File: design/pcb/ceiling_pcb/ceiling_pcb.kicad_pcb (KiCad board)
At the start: 2 copper layers, 60 x 208 mm, 10 parts, among them J1 Conn_01x09, J10 shock_grid, J2 Conn_01x09, J3 shock_grid, J4 shock_grid, J5 shock_grid, J6 shock_grid, J7 shock_grid, J8 shock_grid, J9 shock_grid

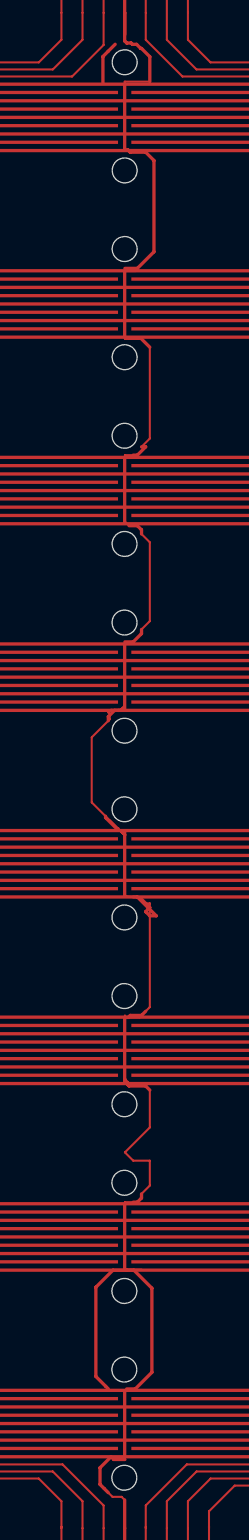
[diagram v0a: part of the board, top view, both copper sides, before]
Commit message: Think ceiling has holes converted to a manufacturable format. Going to do floor now then regenerate output for manufacture.
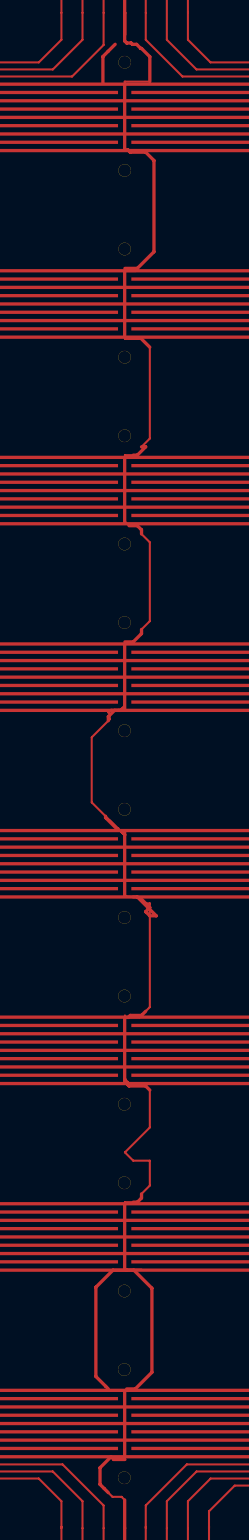
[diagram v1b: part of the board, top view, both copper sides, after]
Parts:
- added R1.5mm_NPTH: , R1.5mm_NPTH, F.Cu at (125.0, 29.7)
- added R1.5mm_NPTH: , R1.5mm_NPTH, F.Cu at (125.0, 132.8)
- added R1.5mm_NPTH: , R1.5mm_NPTH, F.Cu at (125.0, 142.2)
- added R1.5mm_NPTH: , R1.5mm_NPTH, F.Cu at (125.0, 155.3)
- added R1.5mm_NPTH: , R1.5mm_NPTH, F.Cu at (125.0, 164.7)
- added R1.5mm_NPTH: , R1.5mm_NPTH, F.Cu at (125.0, 177.8)
- added R1.5mm_NPTH: , R1.5mm_NPTH, F.Cu at (125.0, 187.2)
- added R1.5mm_NPTH: , R1.5mm_NPTH, F.Cu at (125.0, 200.3)
- added R1.5mm_NPTH: , R1.5mm_NPTH, F.Cu at (125.0, 42.8)
- added R1.5mm_NPTH: , R1.5mm_NPTH, F.Cu at (125.0, 52.2)
- added R1.5mm_NPTH: , R1.5mm_NPTH, F.Cu at (125.0, 65.3)
- added R1.5mm_NPTH: , R1.5mm_NPTH, F.Cu at (125.0, 87.8)
- added R1.5mm_NPTH: , R1.5mm_NPTH, F.Cu at (125.0, 74.7)
- added R1.5mm_NPTH: , R1.5mm_NPTH, F.Cu at (125.0, 97.2)
- added R1.5mm_NPTH: , R1.5mm_NPTH, F.Cu at (125.0, 110.3)
- added R1.5mm_NPTH: , R1.5mm_NPTH, F.Cu at (125.0, 119.7)
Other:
- outline, holes or cut-outs redrawn
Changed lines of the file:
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@@
-(kicad_pcb (version 20170922) (host pcbnew "(2017-11-10 revision d8f4e35)-HEAD")
+(kicad_pcb (version 20171130) (host pcbnew "(2017-12-12 revision 8e764f8)-master")
   (general
     (thickness 1.6)
-    (drawings 24)
+    (drawings 8)
     (tracks 283)
     (zones 0)
-    (modules 10)
+    (modules 26)
     (nets 18)
   )
@@
     (add_net /HV)
   )
+  (module R1.5mm_NPTH locked (layer F.Cu)
+    (at 125.001 29.7452)
+    (tags "non-plated through hole NPTH")
+    (attr virtual)
+    (fp_text reference R1.5mm_NPTH (at 0 0) (layer Cmts.User)
+      (effects (font (thickness 0.15)))
+    )
+    (fp_text value "" (at 0 0) (layer Cmts.User)
+      (effects (font (thickness 0.15)))
+    )
+    (pad 1 np_thru_hole circle (at 0 0) (size 1.524 1.524) (drill 1.5) (layers *.Cu *.Mask))
+  )
+  (module R1.5mm_NPTH locked (layer F.Cu)
+    (at 125.001 42.7792)
+    (tags "non-plated through hole NPTH")
+    (attr virtual)
+    (fp_text reference R1.5mm_NPTH (at 0 0) (layer Cmts.User)
+      (effects (font (thickness 0.15)))
+    )
+    (fp_text value "" (at 0 0) (layer Cmts.User)
+      (effects (font (thickness 0.15)))
+    )
+    (pad 1 np_thru_hole circle (at 0 0) (size 1.524 1.524) (drill 1.5) (layers *.Cu *.Mask))
+  )
+  (module R1.5mm_NPTH locked (layer F.Cu)
+    (at 124.995 52.2452)
+    (tags "non-plated through hole NPTH")
+    (attr virtual)
+    (fp_text reference R1.5mm_NPTH (at 0 0) (layer Cmts.User)
+      (effects (font (thickness 0.15)))
+    )
+    (fp_text value "" (at 0 0) (layer Cmts.User)
+      (effects (font (thickness 0.15)))
+    )
+    (pad 1 np_thru_hole circle (at 0 0) (size 1.524 1.524) (drill 1.5) (layers *.Cu *.Mask))
+  )
+  (module R1.5mm_NPTH locked (layer F.Cu)
+    (at 124.995 65.2792)
+    (tags "non-plated through hole NPTH")
+    (attr virtual)
+    (fp_text reference R1.5mm_NPTH (at 0 0) (layer Cmts.User)
+      (effects (font (thickness 0.15)))
+    )
+    (fp_text value "" (at 0 0) (layer Cmts.User)
+      (effects (font (thickness 0.15)))
+    )
+    (pad 1 np_thru_hole circle (at 0 0) (size 1.524 1.524) (drill 1.5) (layers *.Cu *.Mask))
+  )
+  (module R1.5mm_NPTH locked (layer F.Cu)
+    (at 124.989 87.7792)
+    (tags "non-plated through hole NPTH")
+    (attr virtual)
+    (fp_text reference R1.5mm_NPTH (at 0 0) (layer Cmts.User)
+      (effects (font (thickness 0.15)))
+    )
+    (fp_text value "" (at 0 0) (layer Cmts.User)
+      (effects (font (thickness 0.15)))
+    )
+    (pad 1 np_thru_hole circle (at 0 0) (size 1.524 1.524) (drill 1.5) (layers *.Cu *.Mask))
+  )
+  (module R1.5mm_NPTH locked (layer F.Cu)
+    (at 124.989 74.7452)
+    (tags "non-plated through hole NPTH")
+    (attr virtual)
+    (fp_text reference R1.5mm_NPTH (at 0 0) (layer Cmts.User)
+      (effects (font (thickness 0.15)))
+    )
+    (fp_text value "" (at 0 0) (layer Cmts.User)
+      (effects (font (thickness 0.15)))
+    )
+    (pad 1 np_thru_hole circle (at 0 0) (size 1.524 1.524) (drill 1.5) (layers *.Cu *.Mask))
+  )
+  (module R1.5mm_NPTH locked (layer F.Cu)
+    (at 124.983 97.2452)
+    (tags "non-plated through hole NPTH")
+    (attr virtual)
+    (fp_text reference R1.5mm_NPTH (at 0 0) (layer Cmts.User)
+      (effects (font (thickness 0.15)))
+    )
+    (fp_text value "" (at 0 0) (layer Cmts.User)
+      (effects (font (thickness 0.15)))
+    )
+    (pad 1 np_thru_hole circle (at 0 0) (size 1.524 1.524) (drill 1.5) (layers *.Cu *.Mask))
+  )
+  (module R1.5mm_NPTH locked (layer F.Cu)
+    (at 124.983 110.2795)
+    (tags "non-plated through hole NPTH")
+    (attr virtual)
+    (fp_text reference R1.5mm_NPTH (at 0 0) (layer Cmts.User)
+      (effects (font (thickness 0.15)))
+    )
+    (fp_text value "" (at 0 0) (layer Cmts.User)
+      (effects (font (thickness 0.15)))
+    )
+    (pad 1 np_thru_hole circle (at 0 0) (size 1.524 1.524) (drill 1.5) (layers *.Cu *.Mask))
+  )
+  (module R1.5mm_NPTH locked (layer F.Cu)
+    (at 124.977 119.7455)
+    (tags "non-plated through hole NPTH")
+    (attr virtual)
+    (fp_text reference R1.5mm_NPTH (at 0 0) (layer Cmts.User)
+      (effects (font (thickness 0.15)))
+    )
+    (fp_text value "" (at 0 0) (layer Cmts.User)
+      (effects (font (thickness 0.15)))
+    )
+    (pad 1 np_thru_hole circle (at 0 0) (size 1.524 1.524) (drill 1.5) (layers *.Cu *.Mask))
+  )
+  (module R1.5mm_NPTH locked (layer F.Cu)
+    (at 124.977 132.7796)
+    (tags "non-plated through hole NPTH")
+    (attr virtual)
+    (fp_text reference R1.5mm_NPTH (at 0 0) (layer Cmts.User)
+      (effects (font (thickness 0.15)))
+    )
+    (fp_text value "" (at 0 0) (layer Cmts.User)
+      (effects (font (thickness 0.15)))
+    )
+    (pad 1 np_thru_hole circle (at 0 0) (size 1.524 1.524) (drill 1.5) (layers *.Cu *.Mask))
+  )
+  (module R1.5mm_NPTH locked (layer F.Cu)
+    (at 124.971 142.2456)
+    (tags "non-plated through hole NPTH")
+    (attr virtual)
+    (fp_text reference R1.5mm_NPTH (at 0 0) (layer Cmts.User)
+      (effects (font (thickness 0.15)))
+    )
+    (fp_text value "" (at 0 0) (layer Cmts.User)
+      (effects (font (thickness 0.15)))
+    )
+    (pad 1 np_thru_hole circle (at 0 0) (size 1.524 1.524) (drill 1.5) (layers *.Cu *.Mask))
+  )
+  (module R1.5mm_NPTH locked (layer F.Cu)
+    (at 124.971 155.2796)
+    (tags "non-plated through hole NPTH")
+    (attr virtual)
+    (fp_text reference R1.5mm_NPTH (at 0 0) (layer Cmts.User)
+      (effects (font (thickness 0.15)))
+    )
+    (fp_text value "" (at 0 0) (layer Cmts.User)
+      (effects (font (thickness 0.15)))
+    )
+    (pad 1 np_thru_hole circle (at 0 0) (size 1.524 1.524) (drill 1.5) (layers *.Cu *.Mask))
+  )
+  (module R1.5mm_NPTH locked (layer F.Cu)
+    (at 124.965 164.7457)
+    (tags "non-plated through hole NPTH")
+    (attr virtual)
+    (fp_text reference R1.5mm_NPTH (at 0 0) (layer Cmts.User)
+      (effects (font (thickness 0.15)))
+    )
+    (fp_text value "" (at 0 0) (layer Cmts.User)
+      (effects (font (thickness 0.15)))
+    )
+    (pad 1 np_thru_hole circle (at 0 0) (size 1.524 1.524) (drill 1.5) (layers *.Cu *.Mask))
+  )
+  (module R1.5mm_NPTH locked (layer F.Cu)
+    (at 124.965 177.7797)
+    (tags "non-plated through hole NPTH")
+    (attr virtual)
+    (fp_text reference R1.5mm_NPTH (at 0 0) (layer Cmts.User)
+      (effects (font (thickness 0.15)))
+    )
+    (fp_text value "" (at 0 0) (layer Cmts.User)
+      (effects (font (thickness 0.15)))
+    )
+    (pad 1 np_thru_hole circle (at 0 0) (size 1.524 1.524) (drill 1.5) (layers *.Cu *.Mask))
+  )
+  (module R1.5mm_NPTH locked (layer F.Cu)
+    (at 124.959 187.2458)
+    (tags "non-plated through hole NPTH")
+    (attr virtual)
+    (fp_text reference R1.5mm_NPTH (at 0 0) (layer Cmts.User)
+      (effects (font (thickness 0.15)))
+    )
+    (fp_text value "" (at 0 0) (layer Cmts.User)
+      (effects (font (thickness 0.15)))
+    )
+    (pad 1 np_thru_hole circle (at 0 0) (size 1.524 1.524) (drill 1.5) (layers *.Cu *.Mask))
+  )
+  (module R1.5mm_NPTH locked (layer F.Cu)
+    (at 124.959 200.27981)
+    (tags "non-plated through hole NPTH")
+    (attr virtual)
+    (fp_text reference R1.5mm_NPTH (at 0 0) (layer Cmts.User)
+      (effects (font (thickness 0.15)))
+    )
+    (fp_text value "" (at 0 0) (layer Cmts.User)
+      (effects (font (thickness 0.15)))
+    )
+    (pad 1 np_thru_hole circle (at 0 0) (size 1.524 1.524) (drill 1.5) (layers *.Cu *.Mask))
+  )
   (module footprints:contacts_9_P2.54mm_L6mm_W1.94mm (layer F.Cu)
     (at 125 213.75 180)
@@
   (gr_line (start 155 11.025) (end 95 11.025) (layer Edge.Cuts) (width 0.001))
   (gr_line (start 95 219) (end 155 219) (layer Edge.Cuts) (width 0.001))
-  (gr_circle (center 124.959 200.27981) (end 126.459 200.27981) (layer Edge.Cuts) (width 0.001))
-  (gr_circle (center 124.959 187.2458) (end 126.459 187.2458) (layer Edge.Cuts) (width 0.001))
-  (gr_circle (center 124.965 177.7797) (end 126.465 177.7797) (layer Edge.Cuts) (width 0.001))
-  (gr_circle (center 124.965 164.7457) (end 126.465 164.7457) (layer Edge.Cuts) (width 0.001))
-  (gr_circle (center 124.971 155.2796) (end 126.471 155.2796) (layer Edge.Cuts) (width 0.001))
-  (gr_circle (center 124.971 142.2456) (end 126.471 142.2456) (layer Edge.Cuts) (width 0.001))
-  (gr_circle (center 124.977 132.7796) (end 126.477 132.7796) (layer Edge.Cuts) (width 0.001))
-  (gr_circle (center 124.977 119.7455) (end 126.477 119.7455) (layer Edge.Cuts) (width 0.001))
-  (gr_circle (center 124.983 110.2795) (end 126.483 110.2795) (layer Edge.Cuts) (width 0.001))
-  (gr_circle (center 124.983 97.2452) (end 126.483 97.2452) (layer Edge.Cuts) (width 0.001))
-  (gr_circle (center 124.989 74.7452) (end 126.489 74.7452) (layer Edge.Cuts) (width 0.001))
-  (gr_circle (center 124.989 87.7792) (end 126.489 87.7792) (layer Edge.Cuts) (width 0.001))
-  (gr_circle (center 124.995 65.2792) (end 126.495 65.2792) (layer Edge.Cuts) (width 0.001))
-  (gr_circle (center 124.995 52.2452) (end 126.495 52.2452) (layer Edge.Cuts) (width 0.001))
-  (gr_circle (center 125.001 42.7792) (end 126.501 42.7792) (layer Edge.Cuts) (width 0.001))
-  (gr_circle (center 125.001 29.7452) (end 126.501 29.7452) (layer Edge.Cuts) (width 0.001))
   (segment (start 96.57497 96.72497) (end 96.57497 30.581318) (width 0.25) (layer F.Cu) (net 1))
   (segment (start 96.57497 30.581318) (end 110.770488 16.3858) (width 0.25) (layer F.Cu) (net 1))

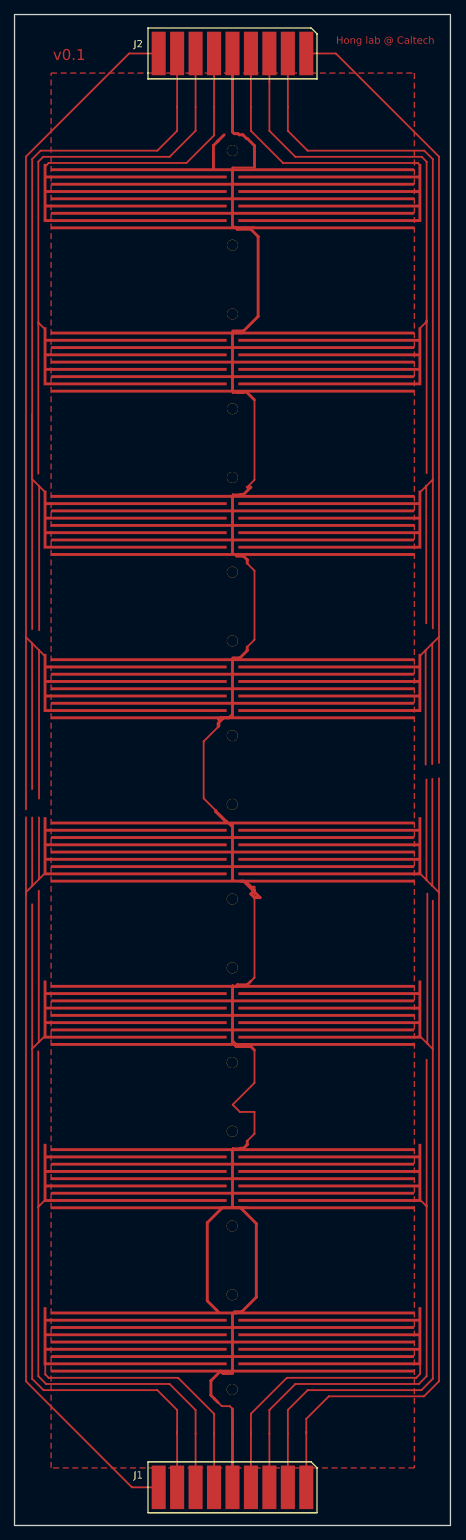
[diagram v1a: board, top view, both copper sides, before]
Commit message: Made ceiling wider in DXF to just barely fit traces. Added floor PCB mounting holes.
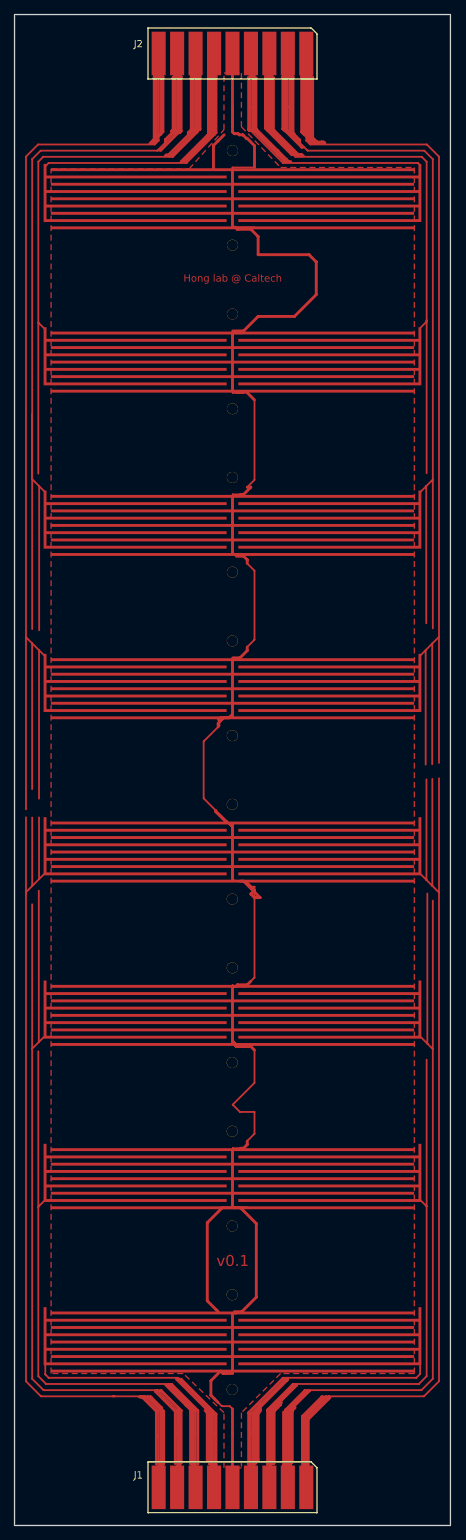
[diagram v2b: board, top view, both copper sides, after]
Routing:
- net /F7: track 143.6 -> 217.0 mm
- net /F2: track 36.3 -> 92.9 mm
- net /F16: track 37.2 -> 93.2 mm
- net /F3: track 78.2 -> 131.4 mm
- net /F6: track 128.2 -> 179.4 mm
- net /F15: track 37.3 -> 87.9 mm
- net /F11: track 121.5 -> 170.2 mm
- net /F8: track 158.1 -> 205.1 mm
- net /F4: track 78.3 -> 123.9 mm
- net /F14: track 80.3 -> 124.8 mm
- net /F13: track 79.1 -> 122.3 mm
- net /F10: track 123.9 -> 165.7 mm
- net /F5: track 118.2 -> 159.0 mm
- net /F1: track 35.9 -> 75.8 mm
- net /F9: track 145.5 -> 184.5 mm
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
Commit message: Imported new ceiling edges to kicad. Too short, but will go ahead and make this way. Not sure full length for pads would fit w/ DSUB
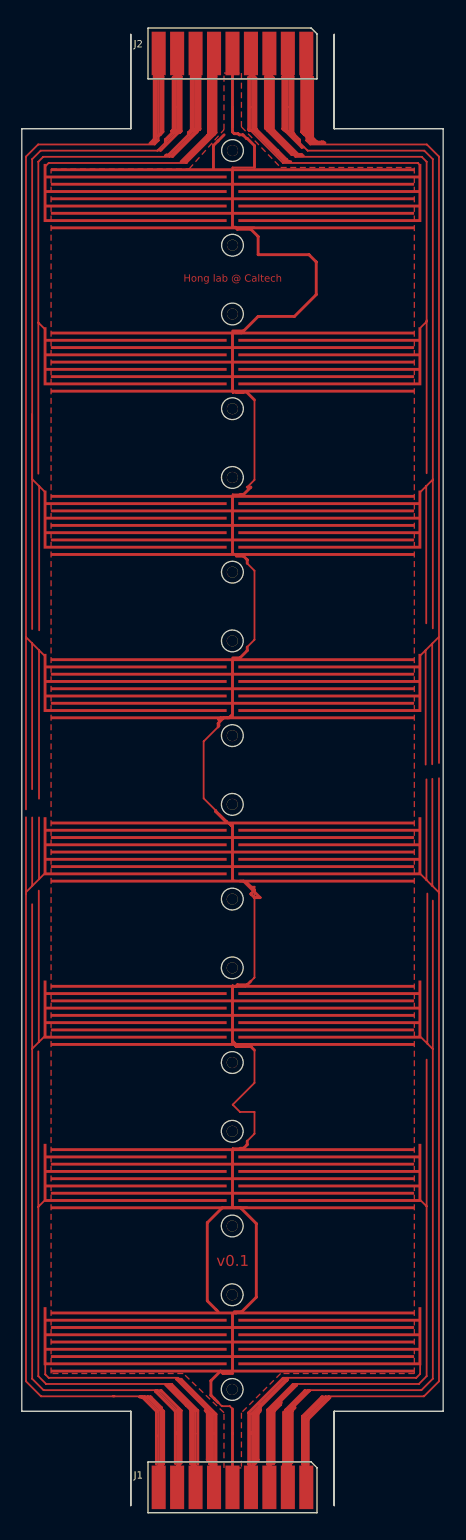
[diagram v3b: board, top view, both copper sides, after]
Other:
- board size 60 x 208 mm -> 58 x 202.5 mm
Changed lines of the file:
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@@
   (general
     (thickness 1.6)
-    (drawings 8)
+    (drawings 42)
     (tracks 605)
     (zones 0)
@@
     (zone_45_only no)
     (trace_min 0.2)
-    (segment_width 0.2)
+    (segment_width 0.001)
     (edge_width 0.001)
     (via_size 0.8)
@@
       ))
   )
+  (gr_line (start 96 203.2798) (end 111 203.2798) (layer Edge.Cuts) (width 0.001))
+  (gr_line (start 96 26.7452) (end 96 203.2798) (layer Edge.Cuts) (width 0.001))
+  (gr_line (start 139 203.2798) (end 154 203.2798) (layer Edge.Cuts) (width 0.001))
+  (gr_line (start 139 216.2798) (end 139 203.2798) (layer Edge.Cuts) (width 0.001))
+  (gr_line (start 111 216.2798) (end 139 216.2798) (layer B.Fab) (width 0.001))
+  (gr_line (start 111 203.2798) (end 111 216.2798) (layer Edge.Cuts) (width 0.001))
+  (gr_line (start 139 13.7452) (end 139 26.7452) (layer Edge.Cuts) (width 0.001))
+  (gr_line (start 111 13.7452) (end 139 13.7452) (layer B.Fab) (width 0.001))
+  (gr_line (start 111 216.2798) (end 111 203.2798) (layer Edge.Cuts) (width 0.001))
+  (gr_line (start 111 216.2798) (end 111 216.2798) (layer Edge.Cuts) (width 0.001))
+  (gr_circle (center 124.989025 74.745375) (end 126.489025 74.745375) (layer Edge.Cuts) (width 0.001))
+  (gr_circle (center 124.989025 87.779375) (end 126.489025 87.779375) (layer Edge.Cuts) (width 0.001))
+  (gr_circle (center 124.995012 52.245288) (end 126.495012 52.245288) (layer Edge.Cuts) (width 0.001))
+  (gr_circle (center 124.995012 65.279288) (end 126.495012 65.279288) (layer Edge.Cuts) (width 0.001))
+  (gr_circle (center 125.001 29.7452) (end 126.501 29.7452) (layer Edge.Cuts) (width 0.001))
+  (gr_line (start 139 216.2798) (end 111 216.2798) (layer B.Fab) (width 0.001))
+  (gr_line (start 139 203.2798) (end 139 216.2798) (layer Edge.Cuts) (width 0.001))
+  (gr_line (start 111 203.2798) (end 139 203.2798) (layer B.Fab) (width 0.001))
+  (gr_line (start 111 26.7452) (end 96 26.7452) (layer Edge.Cuts) (width 0.001))
+  (gr_circle (center 124.971061 155.279638) (end 126.471061 155.279638) (layer Edge.Cuts) (width 0.001))
+  (gr_circle (center 124.977049 119.745551) (end 126.477049 119.745551) (layer Edge.Cuts) (width 0.001))
+  (gr_circle (center 124.977049 132.779551) (end 126.477049 132.779551) (layer Edge.Cuts) (width 0.001))
+  (gr_circle (center 124.983037 97.245463) (end 126.483037 97.245463) (layer Edge.Cuts) (width 0.001))
+  (gr_circle (center 124.983037 110.279463) (end 126.483037 110.279463) (layer Edge.Cuts) (width 0.001))
+  (gr_circle (center 124.959086 187.245814) (end 126.459086 187.245814) (layer Edge.Cuts) (width 0.001))
+  (gr_circle (center 124.959086 200.279814) (end 126.459086 200.279814) (layer Edge.Cuts) (width 0.001))
+  (gr_circle (center 124.965074 164.745726) (end 126.465074 164.745726) (layer Edge.Cuts) (width 0.001))
+  (gr_circle (center 124.965074 177.779726) (end 126.465074 177.779726) (layer Edge.Cuts) (width 0.001))
+  (gr_circle (center 124.971061 142.245638) (end 126.471061 142.245638) (layer Edge.Cuts) (width 0.001))
+  (gr_line (start 111 13.7452) (end 111 26.7452) (layer Edge.Cuts) (width 0.001))
+  (gr_line (start 139 13.7452) (end 111 13.7452) (layer B.Fab) (width 0.001))
+  (gr_line (start 139 26.7452) (end 139 13.7452) (layer Edge.Cuts) (width 0.001))
+  (gr_line (start 154 26.7452) (end 139 26.7452) (layer Edge.Cuts) (width 0.001))
+  (gr_line (start 154 203.2798) (end 154 26.7452) (layer Edge.Cuts) (width 0.001))
+  (gr_circle (center 125.001 42.7792) (end 126.501 42.7792) (layer Edge.Cuts) (width 0.001))
+  (gr_line (start 111 26.7452) (end 111 13.7452) (layer Edge.Cuts) (width 0.001))
+  (gr_line (start 111 26.7452) (end 111 26.7452) (layer Edge.Cuts) (width 0.001))
+  (gr_line (start 139 26.7452) (end 111 26.7452) (layer B.Fab) (width 0.001))
   (gr_text "Board should ideally be 1/8\" (3.175 mm) thick.\n\nOther thicknesses may require different clamps\nto hold ceiling and all layers tight, such that there\nare no gaps due to warping.\n\n\n\n\nThe substrate should be clear, transmitting as much\nIR light as possible.  We used 850 nm IR backlights for\nsome experiments.\n\n\n\n\nSince all the conductors in this board are on one side,\nyou should be able to etch it yourself." (at 49.03 53.58) (layer Cmts.User)
     (effects (font (size 1.5 1.5) (thickness 0.3)))
@@
     (effects (font (size 1.5 1.5) (thickness 0.3)))
   )
-  (gr_line (start 155 11.025) (end 155 219) (layer Edge.Cuts) (width 0.001))
-  (gr_line (start 95 219) (end 95 11.025) (layer Edge.Cuts) (width 0.001))
-  (gr_line (start 155 11.025) (end 95 11.025) (layer Edge.Cuts) (width 0.001))
-  (gr_line (start 95 219) (end 155 219) (layer Edge.Cuts) (width 0.001))
   (segment (start 114.23 28.18) (end 113.63 28.78) (width 0.4) (layer F.Cu) (net 1))
   (segment (start 114.23 19.58) (end 114.23 28.18) (width 0.4) (layer F.Cu) (net 1))
